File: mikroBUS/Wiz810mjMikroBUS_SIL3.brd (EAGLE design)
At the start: 67.9 x 48.6 mm, 2 parts

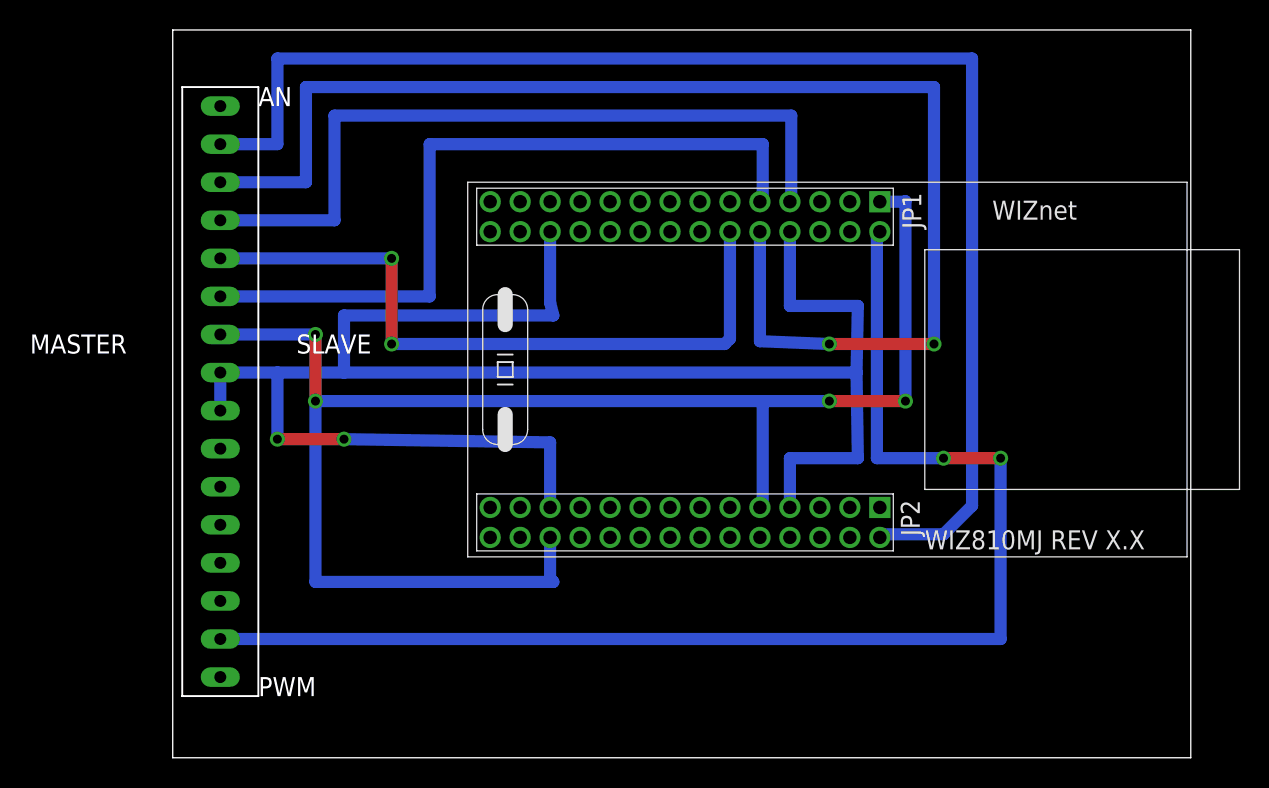
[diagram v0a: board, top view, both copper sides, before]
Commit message: 
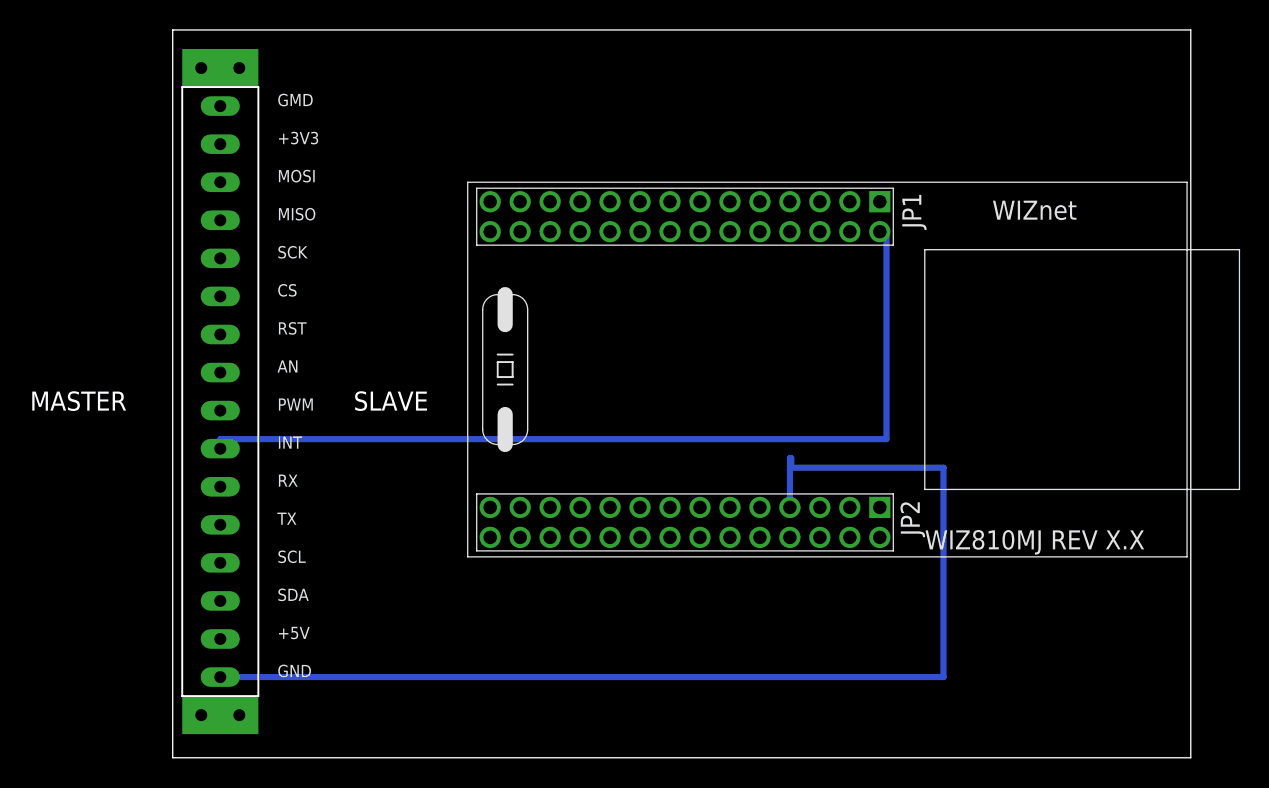
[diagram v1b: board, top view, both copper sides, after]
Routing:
- net N$9: track 103.4 -> 0.00 mm, vias 4 -> 0
- net N$4: track 92.8 -> 0.00 mm
- net N$5: track 90.0 -> 0.00 mm, vias 2 -> 0
- net N$6: track 50.9 -> 0.00 mm
- net N$8: track 50.3 -> 0.00 mm
- net N$7: track 47.0 -> 0.00 mm, vias 2 -> 0
- net N$27: track 122.9 -> 76.4 mm, vias 2 -> 0
- net N$1: track 87.6 -> 59.4 mm, vias 2 -> 0
